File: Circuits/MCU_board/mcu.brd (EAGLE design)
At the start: 100 x 80 mm, 72 parts, among them IC1 RP111N331B-TR-FE, IC2 FT230XS, U1 TCA9548APWR, U2 USBLC6-2P6, U4 LSM9DS1, U5 STM32L452RECT6

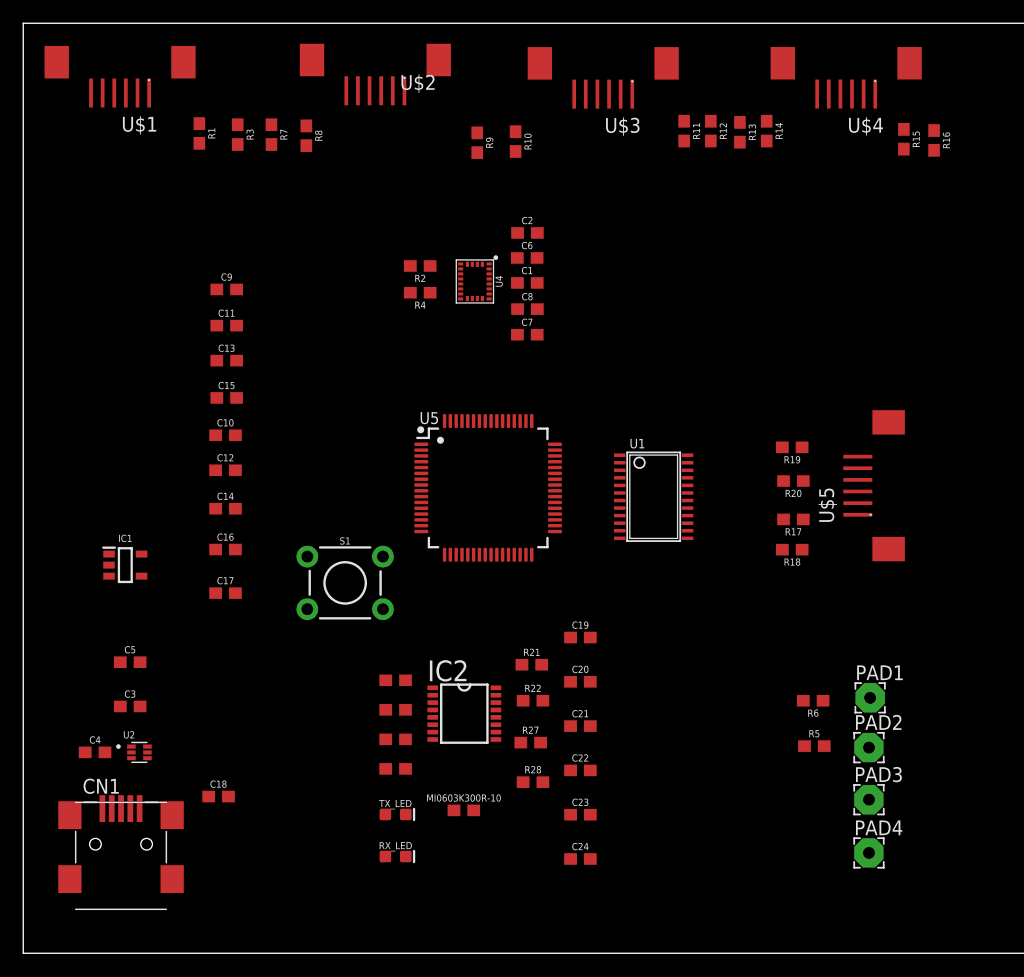
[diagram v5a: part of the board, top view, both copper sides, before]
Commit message: Fixed connector mistakes, preliminary placement of all components
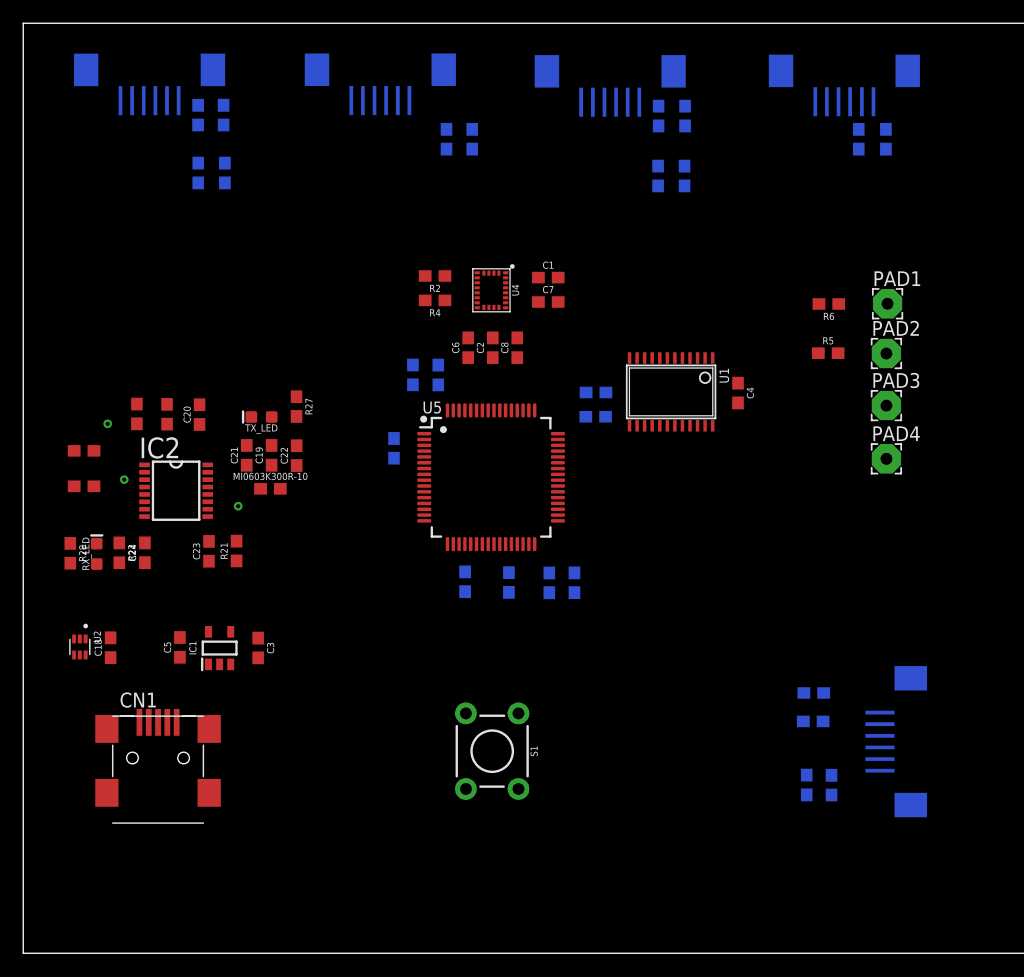
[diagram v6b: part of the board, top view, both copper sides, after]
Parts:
- moved C4 63.4 mm to (61.5, 48.2), turned to 270 degrees
- moved C24 45.8 mm to (10.5, 34.4), turned to 90 degrees
- moved R28 44.4 mm to (4.05, 34.4), turned to 270 degrees
- moved C20 40.0 mm to (15.2, 46.3), turned to 90 degrees
- moved C23 39.2 mm to (16.0, 34.6), turned to 90 degrees
- moved R22 37.8 mm to (8.26, 34.4), turned to 270 degrees
- moved R26 37.8 mm to (9.78, 46.4), turned to 270 degrees
- moved C21 37.0 mm to (19.2, 42.8), turned to 90 degrees
- moved RX_LED 36.6 mm to (6.33, 34.4), turned to 90 degrees
- moved C22 36.5 mm to (23.5, 42.8), turned to 90 degrees
- moved TX_LED 36.1 mm to (20.5, 46.1), turned to 180 degrees
- moved R27 35.2 mm to (23.5, 47.0), turned to 270 degrees
- moved R24 34.8 mm to (5.23, 43.2)
- moved R25 34.5 mm to (5.23, 40.2)
- moved R6 34.2 mm to (69.3, 55.8)
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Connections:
- net N$11 renamed CBUS2
- net N$6 renamed USBDM
- net N$7 renamed USBDP
- net N$9 renamed CBUS1
- removed net N$3: C17.1
- net GND: now also U$1.4, U$2.4, U$3.4, U$4.4, U$5.4; no longer U$1.3, U$2.3, U$3.3, U$4.3, U$5.3
- net NRST: now also C17.1
- net SCL0: now also U$1.6; no longer U$1.1
- net SCL1: now also U$1.2, U$2.2; no longer U$1.5, U$2.5
- net SCL2: now also U$2.6; no longer U$2.1
- net SCL3: now also U$3.6; no longer U$3.1
- net SCL4: now also U$3.2, U$4.2; no longer U$3.5, U$4.5
- net SCL5: now also U$4.6; no longer U$4.1
- net SCL6: now also U$5.6; no longer U$5.1
- net SCL7: now also U$5.2; no longer U$5.5
- net SDA0: now also U$1.5; no longer U$1.2
- net SDA1: now also U$1.1, U$2.1; no longer U$1.6, U$2.6
- net SDA2: now also U$2.5; no longer U$2.2
- net SDA3: now also U$3.5; no longer U$3.2
- net SDA4: now also U$3.1, U$4.1; no longer U$3.6, U$4.6
- net SDA5: now also U$4.5; no longer U$4.2
- net SDA6: now also U$5.5; no longer U$5.2
- net SDA7: now also U$5.1; no longer U$5.6
- net VDD: now also U$1.3, U$2.3, U$3.3, U$4.3, U$5.3; no longer U$1.4, U$2.4, U$3.4, U$4.4, U$5.4

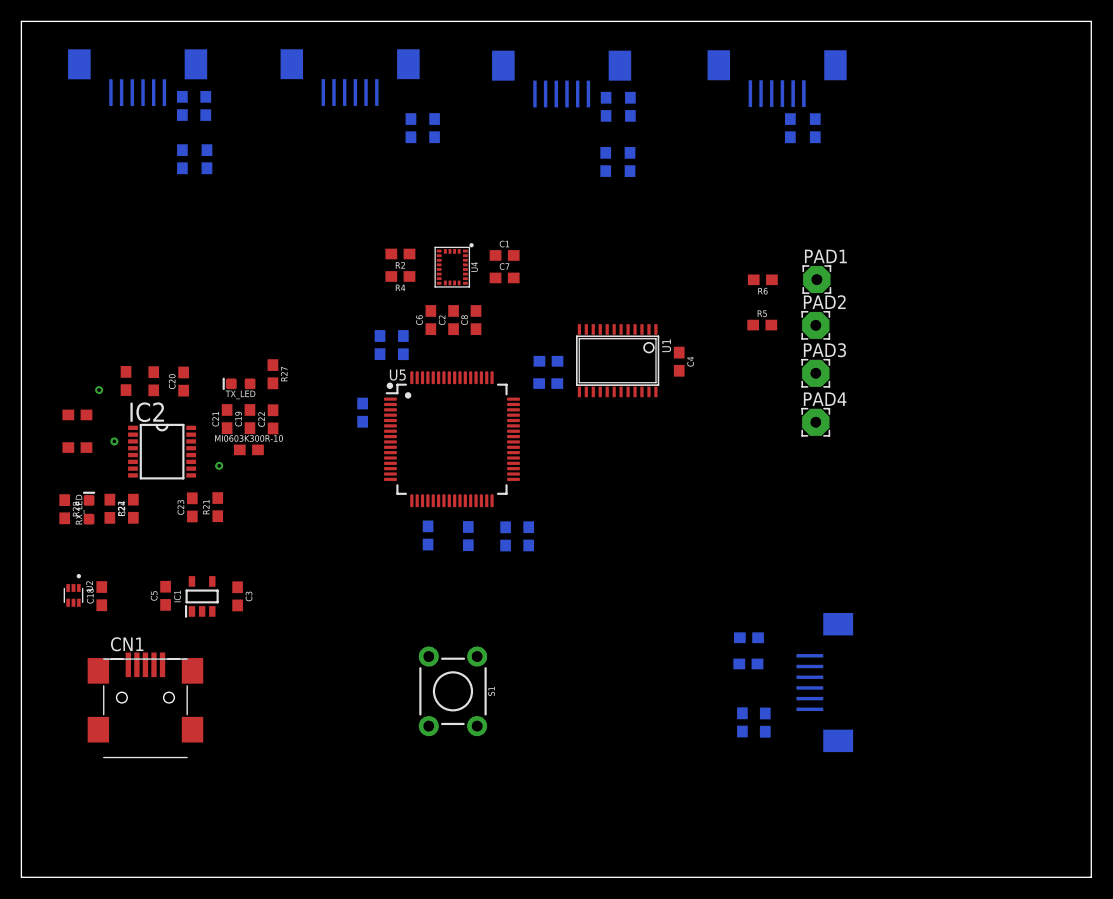
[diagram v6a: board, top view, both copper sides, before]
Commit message: Changed location of components
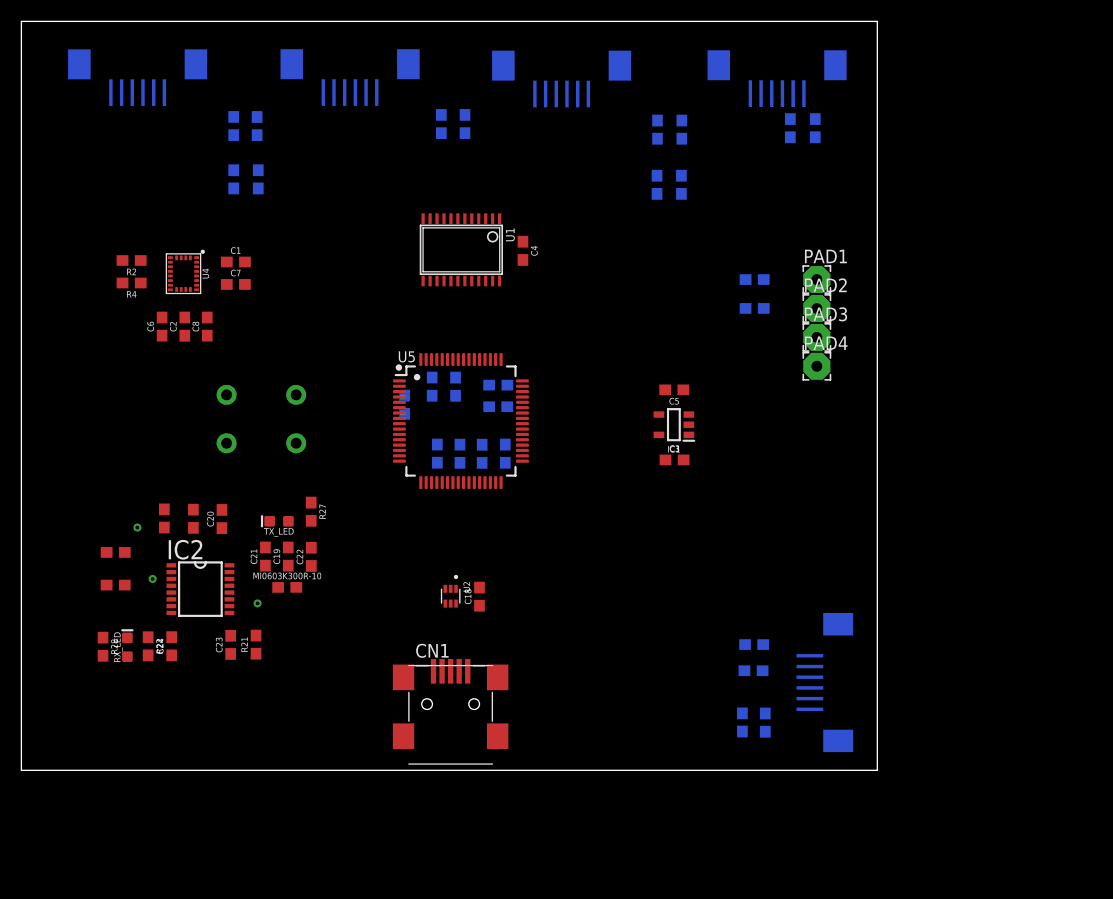
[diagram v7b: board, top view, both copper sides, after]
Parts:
- moved C5 51.3 mm to (61.0, 45.6), turned to 180 degrees
- moved IC1 46.9 mm to (61.0, 42.3), turned to 180 degrees
- moved C3 42.8 mm to (61.1, 39.0), turned to 0 degrees
- moved C18 35.3 mm to (42.8, 26.2)
- moved U2 35.3 mm to (40.1, 26.3)
- moved S1 31.1 mm to (22.4, 42.8), flipped to the bottom, turned to 0 degrees
- moved CN1 28.5 mm to (40.1, 15.2)
- moved C1 25.1 mm to (20.0, 57.5)
- moved C2 25.1 mm to (15.3, 51.5)
- moved C7 25.1 mm to (20.0, 55.4)
- moved C8 25.1 mm to (17.4, 51.5)
- moved R2 25.1 mm to (10.3, 57.6)
- moved R4 25.1 mm to (10.3, 55.5)
- moved C6 25.1 mm to (13.2, 51.5)
- moved U4 25.1 mm to (15.2, 56.4)
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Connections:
- net USB_D+: no longer U5.45
- net USB_D-: no longer U5.44
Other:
- board size 100 x 80 mm -> 80 x 70 mm

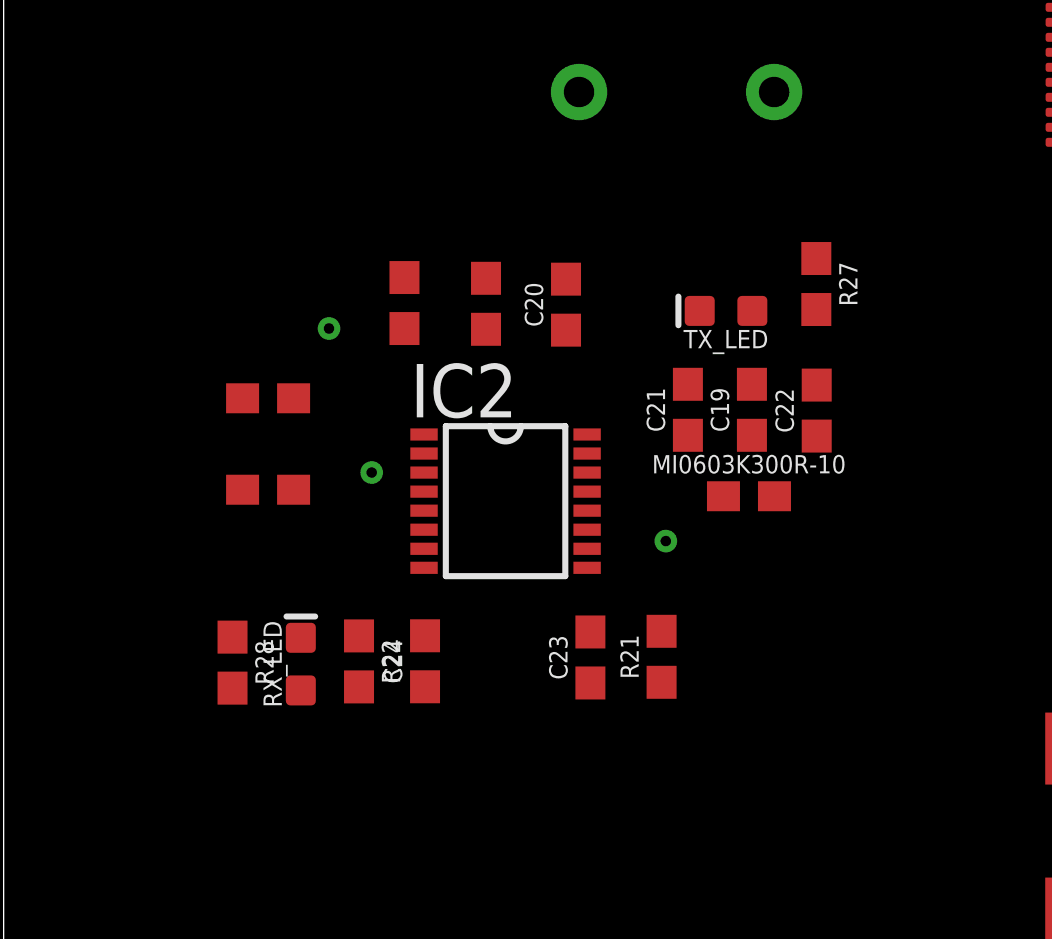
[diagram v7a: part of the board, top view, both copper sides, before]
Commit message: FTDI preliminary routing
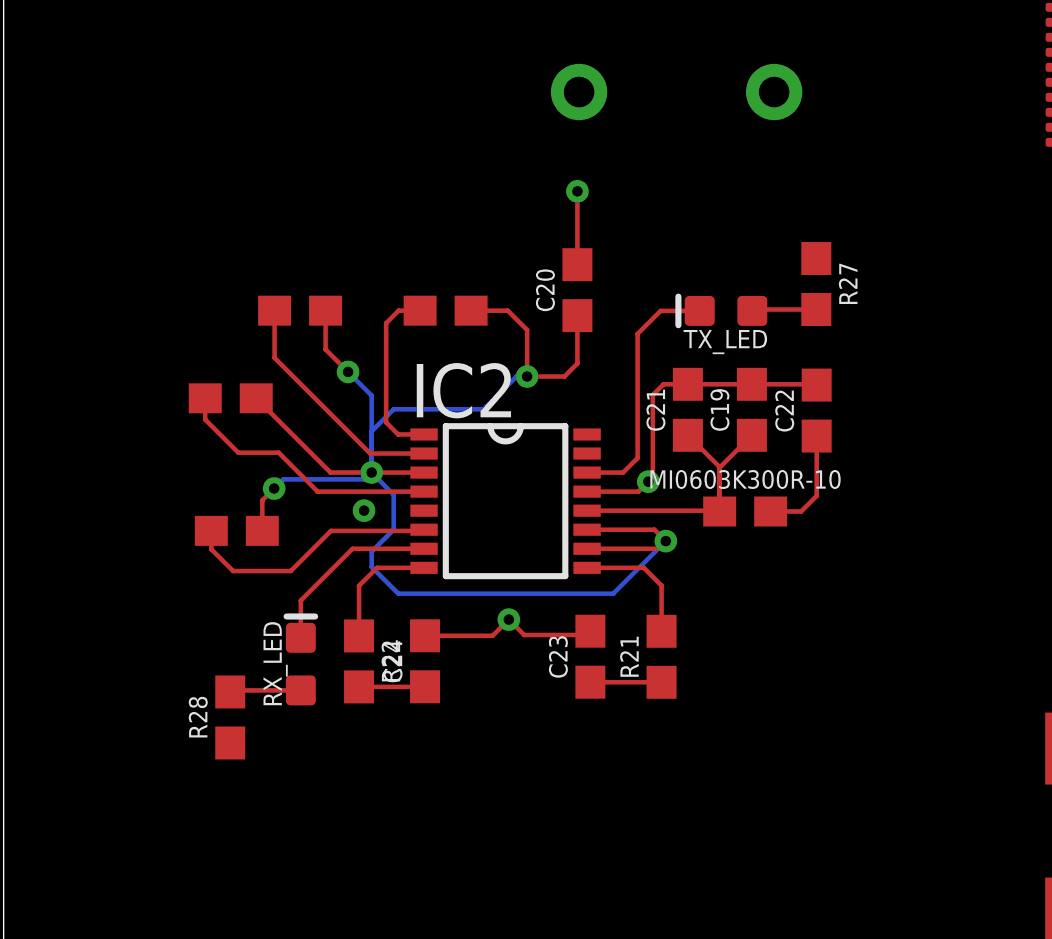
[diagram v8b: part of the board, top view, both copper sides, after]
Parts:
- moved R26 3.49 mm to (9.88, 33.3), turned to 0 degrees
- moved R28 1.83 mm to (7.55, 19.7), turned to 90 degrees
- moved R25 1.72 mm to (7.77, 25.9)
- moved R23 1.37 mm to (14.7, 33.3), turned to 0 degrees
- moved R24 1.24 mm to (7.57, 30.4)
- moved C20 0.61 mm to (19.1, 34.0)
- moved MI0603K300R-10 0.52 mm to (24.7, 26.6)
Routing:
- net VCCIO: track 0.00 -> 52.4 mm, vias 3 -> 5
- net GND: track 0.00 -> 19.2 mm, vias 0 -> 4
- net VCC_USB: track 0.00 -> 10.4 mm
- net RXD: track 0.00 -> 9.00 mm
- net CTS: track 0.00 -> 8.57 mm
- net CBUS1: track 0.00 -> 8.41 mm
- net RTS: track 0.00 -> 7.88 mm
- net CBUS2: track 0.00 -> 6.06 mm
- net TXD: track 0.00 -> 6.04 mm
- net USBDM: track 0.00 -> 4.25 mm
- net USBDP: track 0.00 -> 4.09 mm
- net VBUS: track 0.00 -> 3.74 mm
- net N$10: track 0.00 -> 2.37 mm
- net USB_D-: track 0.00 -> 2.37 mm
- net USB_D+: track 0.00 -> 2.20 mm
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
